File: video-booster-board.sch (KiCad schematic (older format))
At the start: 140 parts, among them IC1 INA180A1IDBVT, J1 0473460001, J10 M20-9990246, J11 MC-HVT1-S04-G, J12 solder_jumper, J13 solder_jumper, J14 solder_jumper, J2 CHDMI-AMSS-01-C, J3 CHDMI-AMSS-01-C, J4 694103107102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

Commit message: Opsis side HDMI connectors changed to 90 deg
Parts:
- removed J2, J3: CHDMI-AMSS-01-C, video-booster-board-footprints:CHDMI-AMSS-01-C, symbol video-booster-board:CHDMI-AMSS-01-C
- added J2, J3: CHDMI-AMSS-01-C-Vertical, antmicro-footprints:CHDMI-AMSS-01-C-Vertical-mod1, symbol antmicroUSBDVIHDMIConnectors:CHDMI-AMSS-01-C-Vertical
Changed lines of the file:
@@
 EESchema Schematic File Version 4
+LIBS:video-booster-board-cache
 EELAYER 30 0
 EELAYER END
@@
 Text Notes 17800 13350 0    138  ~ 28
 Markings
-$Comp
-L video-booster-board:CHDMI-AMSS-01-C J2
-U 1 1 5DE81C03
-P 2100 3400
-F 0 "J2" V 1650 2650 50  0000 R CNN
-F 1 "CHDMI-AMSS-01-C" V 1750 3300 50  0000 R CNN
-F 2 "video-booster-board-footprints:CHDMI-AMSS-01-C" H 2300 3600 60  0001 L CNN
-F 3 "" H 2175 3550 50  0001 C CNN
-	1    2100 3400
-	1    0    0    -1
-$EndComp
-$Comp
-L video-booster-board:CHDMI-AMSS-01-C J3
-U 1 1 5DE89759
-P 2450 10850
-F 0 "J3" V 2000 10100 50  0000 R CNN
-F 1 "CHDMI-AMSS-01-C" V 2100 10750 50  0000 R CNN
-F 2 "video-booster-board-footprints:CHDMI-AMSS-01-C" H 2650 11050 60  0001 L CNN
-F 3 "" H 2525 11000 50  0001 C CNN
-	1    2450 10850
-	1    0    0    -1
-$EndComp
 Wire Wire Line
 	14900 2200 14900 2250
@@
 $EndComp
 Connection ~ 16850 9200
+$Comp
+L antmicroUSBDVIHDMIConnectors:CHDMI-AMSS-01-C-Vertical J2
+U 1 1 5E106A04
+P 2100 3400
+F 0 "J2" V 1650 2700 50  0000 R CNN
+F 1 "CHDMI-AMSS-01-C-Vertical" V 1750 3700 50  0000 R CNN
+F 2 "antmicro-footprints:CHDMI-AMSS-01-C-Vertical-mod1" H 2300 3600 60  0001 L CNN
+F 3 "" H 2175 3550 50  0001 C CNN
+	1    2100 3400
+	1    0    0    -1
+$EndComp
+$Comp
+L antmicroUSBDVIHDMIConnectors:CHDMI-AMSS-01-C-Vertical J3
+U 1 1 5E11114A
+P 2450 10850
+F 0 "J3" V 2000 10150 50  0000 R CNN
+F 1 "CHDMI-AMSS-01-C-Vertical" V 2100 11150 50  0000 R CNN
+F 2 "antmicro-footprints:CHDMI-AMSS-01-C-Vertical-mod1" H 2650 11050 60  0001 L CNN
+F 3 "" H 2525 11000 50  0001 C CNN
+	1    2450 10850
+	1    0    0    -1
+$EndComp
 $EndSCHEMATC

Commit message: Local library updated
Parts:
- J2, J3: footprint antmicro-footprints:CHDMI-AMSS-01-C-Vertical-mod1 -> video-booster-board-footprints:CHDMI-AMSS-01-C-Vertical-mod1; symbol antmicroUSBDVIHDMIConnectors:CHDMI-AMSS-01-C-Vertical -> video-booster-board:CHDMI-AMSS-01-C-Vertical
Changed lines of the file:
@@
 Connection ~ 16850 9200
 $Comp
-L antmicroUSBDVIHDMIConnectors:CHDMI-AMSS-01-C-Vertical J2
+L video-booster-board:CHDMI-AMSS-01-C-Vertical J2
 U 1 1 5E106A04
 P 2100 3400
 F 0 "J2" V 1650 2700 50  0000 R CNN
 F 1 "CHDMI-AMSS-01-C-Vertical" V 1750 3700 50  0000 R CNN
-F 2 "antmicro-footprints:CHDMI-AMSS-01-C-Vertical-mod1" H 2300 3600 60  0001 L CNN
+F 2 "video-booster-board-footprints:CHDMI-AMSS-01-C-Vertical-mod1" H 2300 3600 60  0001 L CNN
 F 3 "" H 2175 3550 50  0001 C CNN
 	1    2100 3400
@@
 $EndComp
 $Comp
-L antmicroUSBDVIHDMIConnectors:CHDMI-AMSS-01-C-Vertical J3
+L video-booster-board:CHDMI-AMSS-01-C-Vertical J3
 U 1 1 5E11114A
 P 2450 10850
 F 0 "J3" V 2000 10150 50  0000 R CNN
 F 1 "CHDMI-AMSS-01-C-Vertical" V 2100 11150 50  0000 R CNN
-F 2 "antmicro-footprints:CHDMI-AMSS-01-C-Vertical-mod1" H 2650 11050 60  0001 L CNN
+F 2 "video-booster-board-footprints:CHDMI-AMSS-01-C-Vertical-mod1" H 2650 11050 60  0001 L CNN
 F 3 "" H 2525 11000 50  0001 C CNN
 	1    2450 10850

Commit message: SWD changed from pinhead to testpads, routing in progress
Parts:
- removed J11: MC-HVT1-S04-G, video-booster-board-footprints:PinHeader_1x4_P1.27mm_Drill.7mm, symbol video-booster-board:MC-HVT1-S04-G-
- added TP1, TP2, TP3, TP4: TP_SMD_0_75MM, antmicro-footprints:Testpoint_smd_0_75mm, symbol antmicroTestPoints:TP_SMD_0_75MM
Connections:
- wire segments 584 -> 585
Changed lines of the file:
@@
 Text Label 17800 11100 0    50   ~ 0
 DBG_SWDIO
-Text Notes 18800 10900 0    50   ~ 0
+Text Notes 19350 11150 0    50   ~ 0
 SWD Debug
-Wire Wire Line
-	18450 11200 18850 11200
-$Comp
-L video-booster-board:MC-HVT1-S04-G- J11
-U 1 1 5F05FE9B
-P 19000 11300
-F 0 "J11" V 19191 11222 50  0000 R CNN
-F 1 "MC-HVT1-S04-G" H 19350 11100 50  0000 R CNN
-F 2 "video-booster-board-footprints:PinHeader_1x4_P1.27mm_Drill.7mm" H 19200 11600 60  0001 L CNN
-F 3 "http://www.farnell.com/datasheets/2605295.pdf" H 19200 11700 60  0001 L CNN
-F 4 "MC-HVT1-S04-G" H 19200 11800 60  0001 L CNN "MPN"
-F 5 "Multicomp" H 19200 11900 60  0001 L CNN "Manufacturer"
-	1    19000 11300
-	0    -1   -1   0
-$EndComp
 Wire Wire Line
 	17700 11100 18850 11100
@@
 	1    0    0    -1
 $EndComp
+$Comp
+L video-booster-board:GND #PWR091
+U 1 1 5E7C37AD
+P 15100 11700
+F 0 "#PWR091" H 15100 11450 50  0001 C CNN
+F 1 "GND" H 15105 11527 50  0000 C CNN
+F 2 "" H 15100 11700 50  0001 C CNN
+F 3 "" H 15100 11700 50  0001 C CNN
+	1    15100 11700
+	1    0    0    -1
+$EndComp
+Wire Wire Line
+	15100 11500 15100 11700
+Wire Wire Line
+	18450 11200 18850 11200
+$Comp
+L antmicroTestPoints:TP_SMD_0_75MM TP1
+U 1 1 5E2A7EA1
+P 18950 11300
+F 0 "TP1" V 18950 11250 50  0000 R CNN
+F 1 "TP_SMD_0_75MM" H 18950 11200 50  0001 C CNN
+F 2 "antmicro-footprints:Testpoint_smd_0_75mm" H 19150 11500 60  0001 L CNN
+F 3 "" H 19150 11600 60  0001 L CNN
+	1    18950 11300
+	0    -1   -1   0
+$EndComp
+$Comp
+L antmicroTestPoints:TP_SMD_0_75MM TP4
+U 1 1 5E2AE023
+P 18950 11200
+F 0 "TP4" V 18950 11150 50  0000 R CNN
+F 1 "TP_SMD_0_75MM" H 18950 11100 50  0001 C CNN
+F 2 "antmicro-footprints:Testpoint_smd_0_75mm" H 19150 11400 60  0001 L CNN
+F 3 "" H 19150 11500 60  0001 L CNN
+	1    18950 11200
+	0    -1   -1   0
+$EndComp
+$Comp
+L antmicroTestPoints:TP_SMD_0_75MM TP3
+U 1 1 5E2AE346
+P 18950 11100
+F 0 "TP3" V 18950 11050 50  0000 R CNN
+F 1 "TP_SMD_0_75MM" H 18950 11000 50  0001 C CNN
+F 2 "antmicro-footprints:Testpoint_smd_0_75mm" H 19150 11300 60  0001 L CNN
+F 3 "" H 19150 11400 60  0001 L CNN
+	1    18950 11100
+	0    -1   -1   0
+$EndComp
+$Comp
+L antmicroTestPoints:TP_SMD_0_75MM TP2
+U 1 1 5E2AE5BD
+P 18950 11000
+F 0 "TP2" V 18950 10950 50  0000 R CNN
+F 1 "TP_SMD_0_75MM" H 18950 10900 50  0001 C CNN
+F 2 "antmicro-footprints:Testpoint_smd_0_75mm" H 19150 11200 60  0001 L CNN
+F 3 "" H 19150 11300 60  0001 L CNN
+	1    18950 11000
+	0    -1   -1   0
+$EndComp
 $EndSCHEMATC

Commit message: Removed barrel jack connector
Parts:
- removed J4: 694103107102, video-booster-board-footprints:69410X107102, symbol video-booster-board:694103107102
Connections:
- wire segments 585 -> 581
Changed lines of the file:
@@
 EESchema Schematic File Version 4
-LIBS:video-booster-board-cache
 EELAYER 30 0
 EELAYER END
@@
 Wire Wire Line
 	14900 1800 14900 1900
-Wire Wire Line
-	14150 1800 14600 1800
-Text Notes 13550 2150 0    50   ~ 0
+Text Notes 13800 2050 0    50   ~ 0
 +5V Auxillary
 $Comp
@@
 $EndComp
 $Comp
-L video-booster-board:GND #PWR061
-U 1 1 62AD30B5
-P 14150 2250
-F 0 "#PWR061" H 14150 2000 50  0001 C CNN
-F 1 "GND" H 14155 2077 50  0000 C CNN
-F 2 "" H 14150 2250 50  0001 C CNN
-F 3 "" H 14150 2250 50  0001 C CNN
-	1    14150 2250
-	1    0    0    -1
-$EndComp
-$Comp
 L video-booster-board:C_4u7_0603- C36
 U 1 1 62A47AFC
@@
 Wire Wire Line
 	14600 1800 14600 2000
-Connection ~ 14600 1800
 Wire Wire Line
 	14600 1800 14900 1800
@@
 	1    0    0    -1
 $EndComp
-Wire Wire Line
-	14150 1900 14150 2000
-Wire Wire Line
-	14150 2000 14150 2250
-Connection ~ 14150 2000
-$Comp
-L video-booster-board:694103107102 J4
-U 1 1 5DECDCEC
-P 14150 1800
-F 0 "J4" H 13950 2100 50  0000 C CNN
-F 1 "694103107102" H 13950 2000 50  0000 C CNN
-F 2 "video-booster-board-footprints:69410X107102" H 14350 1825 50  0001 L BNN
-F 3 "https://www.we-online.de/katalog/datasheet/694103107102.pdf" H 14350 1600 50  0001 L BNN
-F 4 "None" H 14350 1750 50  0001 L BNN "Field4"
-F 5 "694103107102" H 14350 1675 50  0001 L BNN "Field5"
-F 6 "Unavailable" H 14350 1450 50  0001 L BNN "Field6"
-F 7 "Wurth Electronics" H 14350 1525 50  0001 L BNN "Field7"
-F 8 "DC Power jack" H 14350 1875 50  0001 L BNN "Field8"
-	1    14150 1800
-	1    0    0    -1
-$EndComp
-Wire Wire Line
-	14150 1800 14150 1725
-Connection ~ 14150 1800
 Text Label 18500 3350 0    50   ~ 0
 RX_SRC_SDA_3V

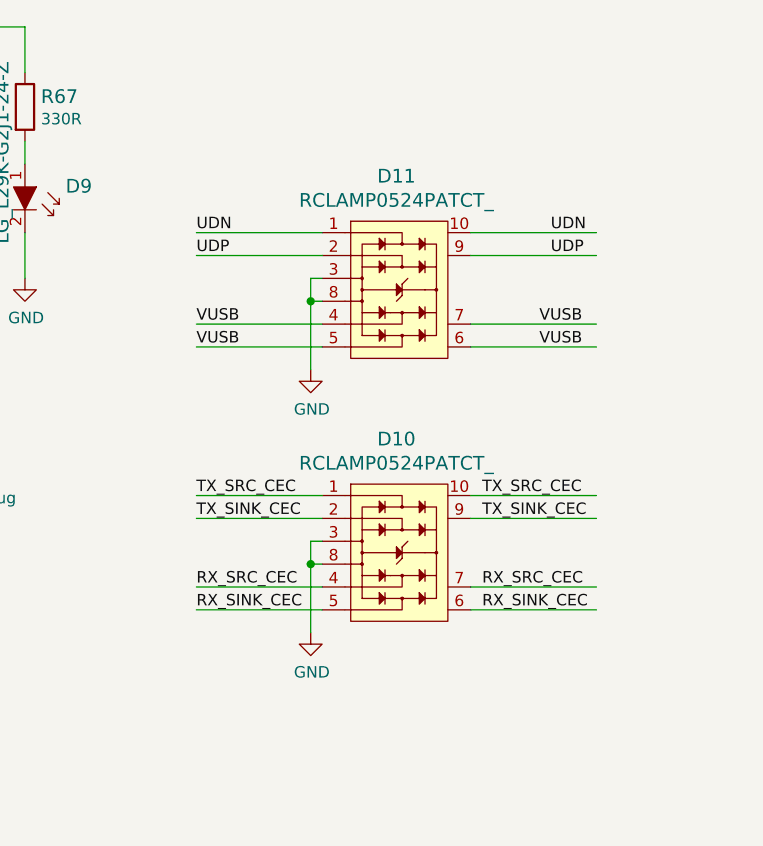
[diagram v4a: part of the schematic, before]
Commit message: Removed TVS, all signalls connected
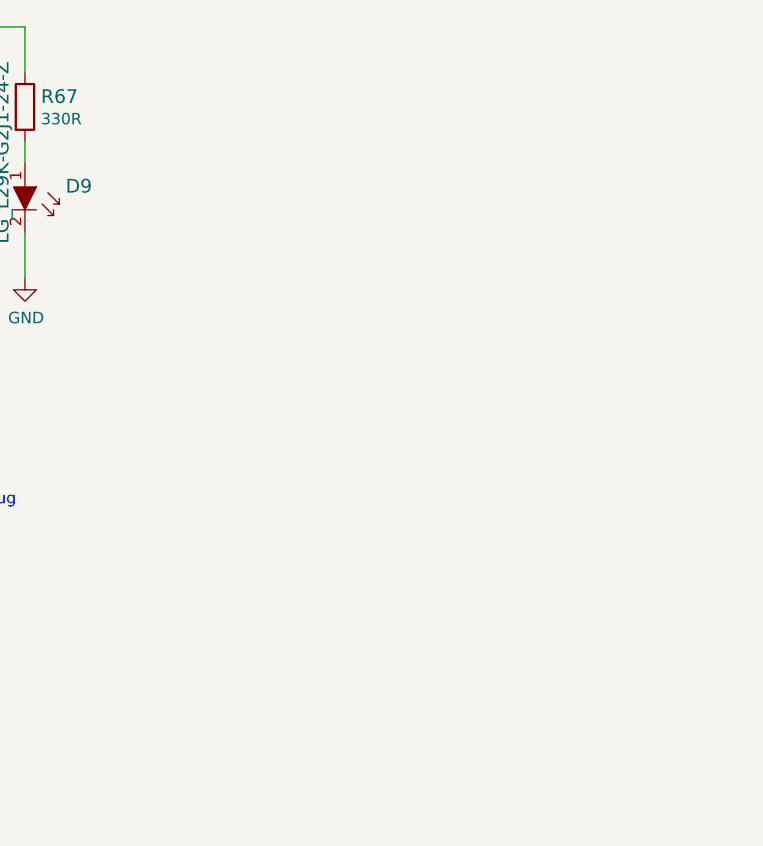
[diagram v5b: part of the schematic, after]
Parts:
- removed D10, D11: RCLAMP0524PATCT_, video-booster-board-footprints:UFDFN-10_2.5x1mm, symbol video-booster-board:RCLAMP0524PATCT_
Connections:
- wire segments 581 -> 557
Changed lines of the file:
@@
 	1    0    0    -1
 $EndComp
-$Comp
-L video-booster-board:GND #PWR079
-U 1 1 5DFE7A15
-P 21050 11700
-F 0 "#PWR079" H 21050 11450 50  0001 C CNN
-F 1 "GND" H 21055 11527 50  0000 C CNN
-F 2 "" H 21050 11700 50  0001 C CNN
-F 3 "" H 21050 11700 50  0001 C CNN
-	1    21050 11700
-	1    0    0    -1
-$EndComp
-Wire Wire Line
-	21100 11500 20550 11500
-Wire Wire Line
-	21100 11600 20550 11600
-Wire Wire Line
-	21100 11200 20550 11200
-Wire Wire Line
-	21100 11100 20550 11100
-Text Label 20550 11100 0    50   ~ 0
-TX_SRC_CEC
-Text Label 20550 11200 0    50   ~ 0
-TX_SINK_CEC
-Text Label 20550 11500 0    50   ~ 0
-RX_SRC_CEC
-Text Label 20550 11600 0    50   ~ 0
-RX_SINK_CEC
-Wire Wire Line
-	22300 11500 21750 11500
-Wire Wire Line
-	22300 11600 21750 11600
-Wire Wire Line
-	22300 11200 21750 11200
-Wire Wire Line
-	22300 11100 21750 11100
-Text Label 21800 11100 0    50   ~ 0
-TX_SRC_CEC
-Text Label 21800 11200 0    50   ~ 0
-TX_SINK_CEC
-Text Label 21800 11500 0    50   ~ 0
-RX_SRC_CEC
-Text Label 21800 11600 0    50   ~ 0
-RX_SINK_CEC
 $Bitmap
 Pos 22600 15100
@@
 EndData
 $EndBitmap
-$Comp
-L video-booster-board:RCLAMP0524PATCT_ D10
-U 1 1 5DDDC206
-P 21600 11400
-F 0 "D10" H 21425 11947 60  0000 C CNN
-F 1 "RCLAMP0524PATCT_" H 21425 11841 60  0000 C CNN
-F 2 "video-booster-board-footprints:UFDFN-10_2.5x1mm" H 20625 10950 60  0001 L CNN
-F 3 "https://www.semtech.com/uploads/documents/rclamp0522p_0524pa.pdf" H 20625 11050 60  0001 L CNN
-F 4 "Semtech Corporation" H 21800 12500 60  0001 L CNN "Manufacturer"
-F 5 "RCLAMP0524PATCT" H 20975 10750 60  0001 L CNN "MPN"
-	1    21600 11400
-	1    0    0    -1
-$EndComp
-Wire Wire Line
-	21100 11300 21050 11300
-Wire Wire Line
-	21050 11300 21050 11400
-Wire Wire Line
-	21100 11400 21050 11400
-Connection ~ 21050 11400
-Wire Wire Line
-	21050 11400 21050 11700
-$Comp
-L video-booster-board:GND #PWR089
-U 1 1 5E01A716
-P 21050 10550
-F 0 "#PWR089" H 21050 10300 50  0001 C CNN
-F 1 "GND" H 21055 10377 50  0000 C CNN
-F 2 "" H 21050 10550 50  0001 C CNN
-F 3 "" H 21050 10550 50  0001 C CNN
-	1    21050 10550
-	1    0    0    -1
-$EndComp
-Wire Wire Line
-	21100 10350 20550 10350
-Wire Wire Line
-	21100 10450 20550 10450
-Wire Wire Line
-	21100 10050 20550 10050
-Wire Wire Line
-	21100 9950 20550 9950
-Wire Wire Line
-	22300 10350 21750 10350
-Wire Wire Line
-	22300 10450 21750 10450
-Wire Wire Line
-	22300 10050 21750 10050
-Wire Wire Line
-	22300 9950 21750 9950
-$Comp
-L video-booster-board:RCLAMP0524PATCT_ D11
-U 1 1 5E01A72E
-P 21600 10250
-F 0 "D11" H 21425 10797 60  0000 C CNN
-F 1 "RCLAMP0524PATCT_" H 21425 10691 60  0000 C CNN
-F 2 "video-booster-board-footprints:UFDFN-10_2.5x1mm" H 20625 9800 60  0001 L CNN
-F 3 "https://www.semtech.com/uploads/documents/rclamp0522p_0524pa.pdf" H 20625 9900 60  0001 L CNN
-F 4 "Semtech Corporation" H 21800 11350 60  0001 L CNN "Manufacturer"
-F 5 "RCLAMP0524PATCT" H 20975 9600 60  0001 L CNN "MPN"
-	1    21600 10250
-	1    0    0    -1
-$EndComp
-Wire Wire Line
-	21100 10150 21050 10150
-Wire Wire Line
-	21050 10150 21050 10250
-Wire Wire Line
-	21100 10250 21050 10250
-Connection ~ 21050 10250
-Wire Wire Line
-	21050 10250 21050 10550
 Text Label 15550 10800 0    50   ~ 0
 UDN
 Text Label 15550 10900 0    50   ~ 0
 UDP
-Text Label 20550 10350 0    50   ~ 0
-VUSB
-Text Label 20550 9950 0    50   ~ 0
-UDN
-Text Label 20550 10050 0    50   ~ 0
-UDP
-Text Label 20550 10450 0    50   ~ 0
-VUSB
-Text Label 22050 10350 0    50   ~ 0
-VUSB
-Text Label 22100 9950 0    50   ~ 0
-UDN
-Text Label 22100 10050 0    50   ~ 0
-UDP
-Text Label 22050 10450 0    50   ~ 0
-VUSB
 $Comp
 L video-booster-board:R_100k_0402- R60

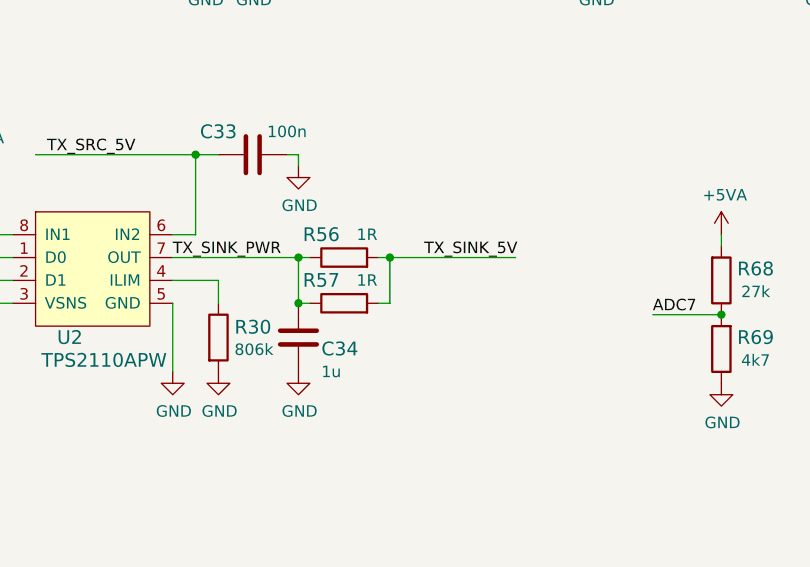
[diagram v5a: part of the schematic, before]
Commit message: Resolved most of DRC errors
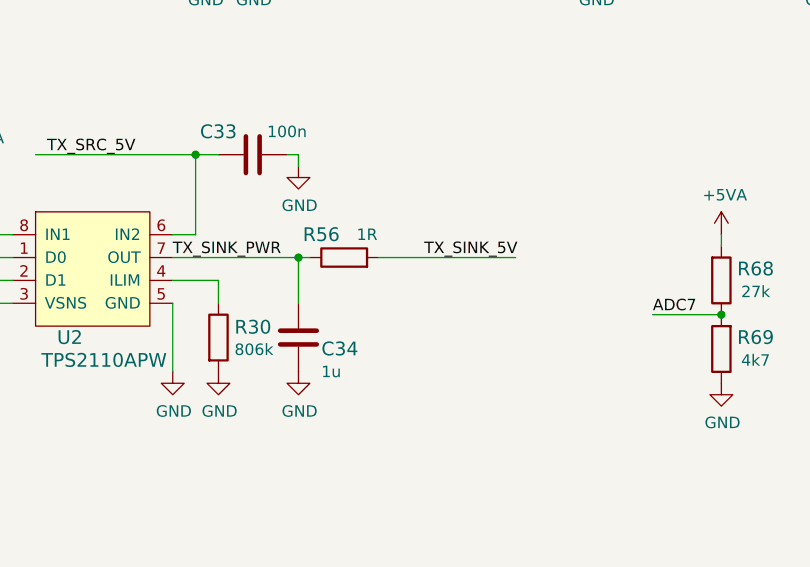
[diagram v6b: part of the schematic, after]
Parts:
- removed R57: R_1R_0402, video-booster-board-footprints:0402-res, symbol video-booster-board:R_1R_0402
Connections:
- wire segments 557 -> 553
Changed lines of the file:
@@
-$EndComp
-$Comp
-L video-booster-board:C_1u_0402- C34
-U 1 1 6348A162
-P 16400 6300
-F 0 "C34" H 16500 6250 60  0000 L CNN
-F 1 "C_1u_0402" H 16400 6150 60  0001 C CNN
-F 2 "video-booster-board-footprints:0402-cap" H 16600 6500 60  0001 L CNN
-F 3 "" H 16400 6300 50  0001 C CNN
-F 4 "TDK" H 16600 6700 60  0001 L CNN "Manufacturer"
-F 5 "C1005X6S1A105K050BC" H 16600 6600 60  0001 L CNN "MPN"
-F 6 "1u" H 16500 6150 50  0000 L CNN "Val"
-	1    16400 6300
-	1    0    0    -1
 $EndComp
 $Comp
@@
 	1    0    0    -1
 $EndComp
-$Comp
-L video-booster-board:R_1R_0402 R57
-U 1 1 63B8103C
-P 16600 6150
-F 0 "R57" H 16500 6250 60  0000 C CNN
-F 1 "R_1R_0402" H 16600 6000 60  0001 C CNN
-F 2 "video-booster-board-footprints:0402-res" H 16800 6350 60  0001 L CNN
-F 3 "" H 16600 6150 50  0001 C CNN
-F 4 "YAGEO" H 16800 6550 60  0001 L CNN "Manufacturer"
-F 5 "RC0402FR-071RL" H 16800 6450 60  0001 L CNN "MPN"
-F 6 "1R" H 16700 6250 50  0000 C CNN "Val"
-	1    16600 6150
-	1    0    0    -1
-$EndComp
 Wire Wire Line
 	16450 5950 16400 5950
 Connection ~ 16400 5950
-Wire Wire Line
-	16400 6150 16450 6150
-Connection ~ 16400 6150
-Wire Wire Line
-	16750 6150 16800 6150
-Wire Wire Line
-	16800 6150 16800 5950
-Wire Wire Line
-	16800 5950 16750 5950
-Connection ~ 16800 5950
 Text Label 15850 5950 0    50   ~ 0
 TX_SINK_PWR
@@
 Text Notes 750  800  0    138  ~ 28
 HDMI transmitter
-Wire Wire Line
-	16800 5950 17350 5950
 Text Label 9850 1850 0    50   ~ 0
 TX_SINK_5V
@@
 	0    -1   -1   0
 $EndComp
+Wire Wire Line
+	16750 5950 17350 5950
+$Comp
+L video-booster-board:C_1u_0402- C34
+U 1 1 6348A162
+P 16400 6300
+F 0 "C34" H 16500 6250 60  0000 L CNN
+F 1 "C_1u_0402" H 16400 6150 60  0001 C CNN
+F 2 "video-booster-board-footprints:0402-cap" H 16600 6500 60  0001 L CNN
+F 3 "" H 16400 6300 50  0001 C CNN
+F 4 "TDK" H 16600 6700 60  0001 L CNN "Manufacturer"
+F 5 "C1005X6S1A105K050BC" H 16600 6600 60  0001 L CNN "MPN"
+F 6 "1u" H 16500 6150 50  0000 L CNN "Val"
+	1    16400 6300
+	1    0    0    -1
+$EndComp
 $EndSCHEMATC
